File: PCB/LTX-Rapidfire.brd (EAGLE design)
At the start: 62.2 x 46.7 mm, 52 parts, among them J1 F-1X08-SIP-100-40Y, Q1 2N3904, Q10 SS8550D, Q11 2N3906, Q12 2N3906, Q13 2N3904, Q2 2N3906, Q3 2N3904, Q4 2N3904, Q5 2N3904, Q6 2N3906, Q7 2N3906, Q8 2N3906, Q9 2N3904, SW1 F-1X02-SIP-100-40, U2 Z8F082ADIL-8

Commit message: Labeled part numbers in schematic. Prep for SMD-ification
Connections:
- net PA0 renamed RELOAD_BUTTON_PA0
- net PA1 renamed INHIBIT_FILTER_PA1
- net PA2 renamed RESET_PA2
- net PA3 renamed LASERMOD_FILTER_PA3
- net PA4 renamed TODI_FILTER_PA4
- net PA5 renamed TIDO_FILTER_PA5

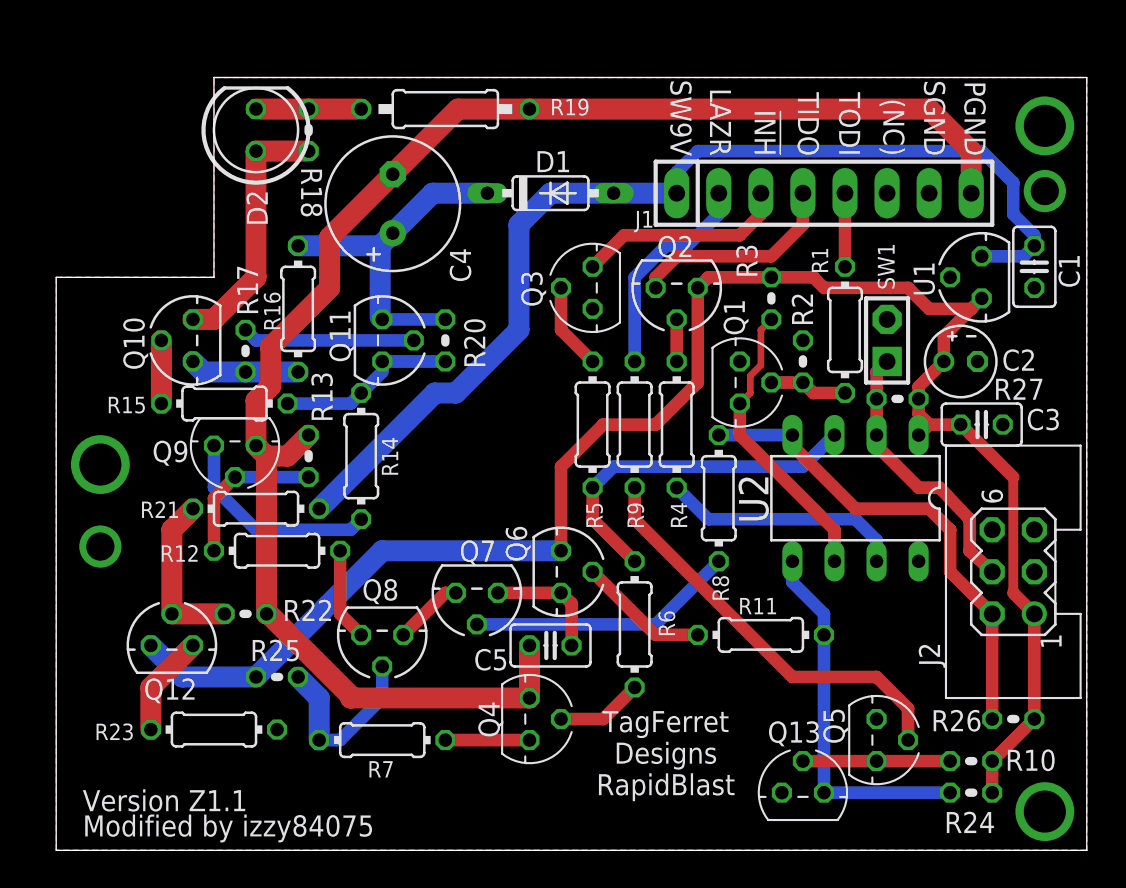
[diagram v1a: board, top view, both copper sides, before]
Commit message: Swapped basics to SMD
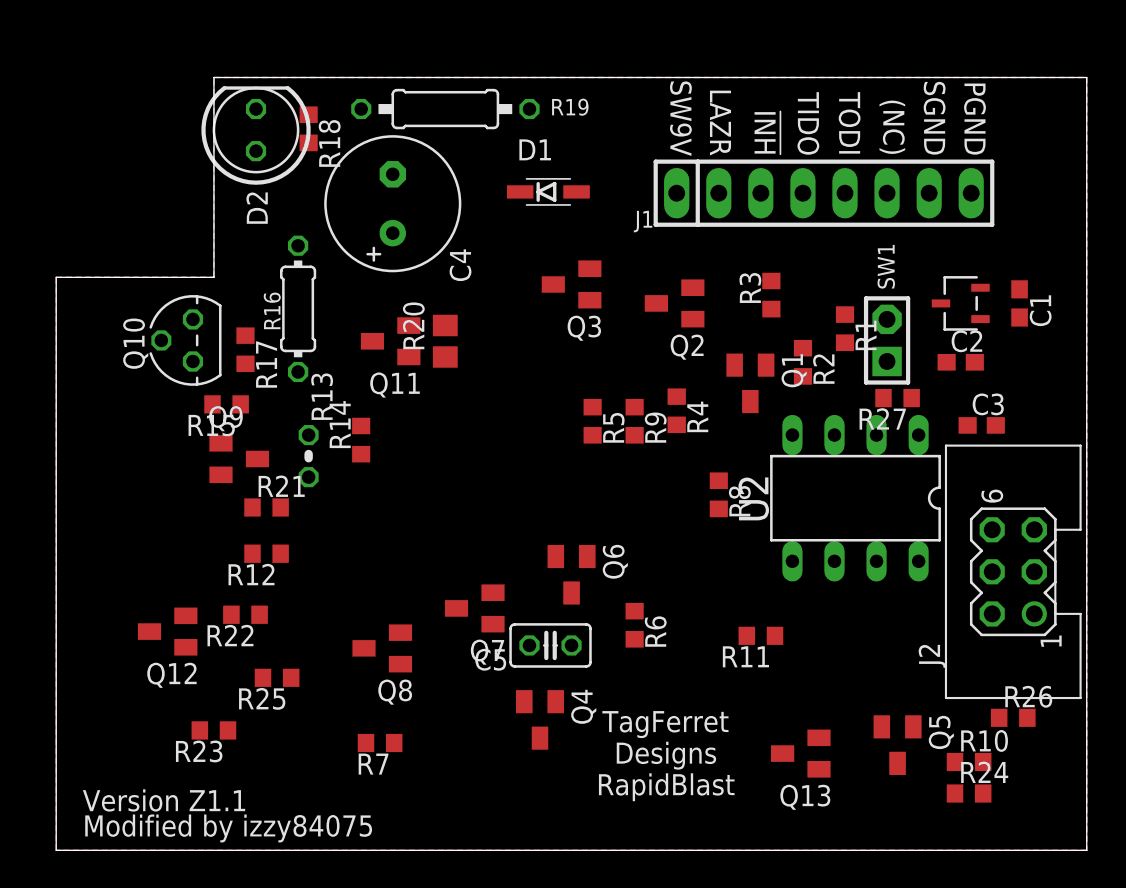
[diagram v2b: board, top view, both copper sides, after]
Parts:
- C1, C3: value 0.1uF -> 100nF; device rcl:C025-025X050 -> JLC PCB Basic Parts_loc:C0603
- C2: value 10uF/10V -> 10uF; device rcl:E2-4 -> JLC PCB Basic Parts_loc:C0603
- D1: value 1N4148DO35-7 -> 1N4148W; device diode:DO35-7 -> JLC PCB Basic Parts_loc:SOD123
- Q1, Q13, Q3, Q4, Q5, Q9: value 2N3904 -> MMBT3904; device transistor:TO92 -> JLC PCB Basic Parts_loc:SOT23
- Q11, Q12, Q2, Q6, Q7, Q8: device transistor-pnp:TO92 -> JLC PCB Basic Parts_loc:SOT23
- R1, R12, R21, R23, R4, R5, R6, R7, R8, R9: device rcl:0204/7 -> JLC PCB Basic Parts_loc:R0603
- R10, R18, R2, R22, R24, R25, R26, R27, R3: device rcl:0204V -> JLC PCB Basic Parts_loc:R0603
- R11: value 1.0k -> 1k; device rcl:0204/7 -> JLC PCB Basic Parts_loc:R0603
- R14: value 150 -> 150R; device rcl:0204/7 -> JLC PCB Basic Parts_loc:R0603
- R15: value 47 -> 47R; device rcl:0204/7 -> JLC PCB Basic Parts_loc:R0603
- R17: value 100 -> 100R; device rcl:0204V -> JLC PCB Basic Parts_loc:R0603
- R20: device rcl:0204V -> JLC PCB Basic Parts_loc:R0805
- U1: value (none) -> XC6206P332MR; device v-reg:78LXX -> LTX-Rapidfire:SOT-23_TOR
- moved C1 2.38 mm to (58.2, 33.0), turned to 270 degrees
- moved Q13 2.37 mm to (45.0, 5.84), turned to 180 degrees
- moved U1 2.02 mm to (54.6, 33.0)
- moved Q5 1.31 mm to (50.8, 6.35)
- moved Q3 1.29 mm to (31.1, 34.2), turned to 180 degrees
- moved R14 0.97 mm to (18.4, 24.8)
- moved Q7 0.95 mm to (25.3, 14.6)
- moved Q2 0.95 mm to (37.3, 33.0)
- moved Q12 0.88 mm to (6.73, 13.2), turned to 180 degrees
- moved Q9 0.85 mm to (11.0, 23.6), turned to 0 degrees
- moved R4 0.84 mm to (37.5, 26.5), turned to 270 degrees
- moved Q8 0.81 mm to (19.7, 12.2)
- moved R12 0.66 mm to (12.7, 17.9), turned to 180 degrees
- moved Q6 0.66 mm to (31.1, 16.6)
- moved R21 0.64 mm to (12.7, 20.7), turned to 0 degrees
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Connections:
- removed net RESET_PA2: J2.2, R26.2, R8.2, U2.4
- removed net TIDO_FILTER_PA5: R4.1, U2.7
- removed net TODI_FILTER_PA4: Q1.1, R3.1, U2.6
- new net PROGRAM_RESET_PA2: J2.2, R26.1, R8.1, U2.4
- new net TIDO_FILTER_TX_PA5: R4.2, U2.7
- new net TODI_FILTER_RX_PA4: Q1.3, R3.1, U2.6
- net INHIBIT: now also Q3.3; no longer Q3.1
- net LASERMOD_FILTER_PA3: now also Q13.3, R11.1; no longer Q13.1, R11.2
- net LAZERMOD: now also R9.1; no longer R9.2
- net N$1: now also Q11.1, R17.1; no longer Q11.2, R17.2
- net N$10: now also Q8.3, R12.1; no longer Q8.1, R12.2
- net N$11: now also Q7.3, Q8.2; no longer Q7.1, Q8.3
- net N$12: now also Q8.1, R7.2; no longer Q8.2, R7.1
- net N$13: now also Q7.1, R8.2; no longer Q7.2, R8.1
- net N$14: now also Q4.3, R7.1; no longer Q4.1, R7.2
- net N$15: now also Q6.3, Q7.2; no longer Q6.1, Q7.3
- net N$16: now also Q4.1; no longer Q4.2
- net N$17: now also Q12.3, R23.2; no longer Q12.1, R23.1
- net N$18: now also Q3.1; no longer Q3.2
- net N$19: now also Q6.1, R11.2; no longer Q6.2, R11.1
- net N$2: now also Q11.2; no longer Q11.3
- net N$20: now also Q12.1, R21.1; no longer Q12.2, R21.2
- net N$21: now also Q13.1, Q5.3; no longer Q13.2, Q5.1
- net N$22: now also Q5.1, R9.2; no longer Q5.2, R9.1
- net N$24: now also Q1.1, R1.2; no longer Q1.2, R1.1
- net N$25: now also Q2.1, R4.1; no longer Q2.2, R4.2
- net N$3: now also R17.2; no longer R17.1
- net N$4: now also Q11.3, R15.1; no longer Q11.1, R15.2
- net N$5: now also R15.2; no longer R15.1
- net N$6: now also Q9.3; no longer Q9.1
- net N$7: now also R18.1; no longer R18.2
- net N$8: now also R18.2; no longer R18.1
- net N$9: now also Q9.1, R12.2; no longer Q9.2, R12.1
- net PGND: now also Q4.2, Q9.2; no longer Q4.3, Q9.3
- net RELOAD_BUTTON_PA0: now also R27.2; no longer R27.1
- net SGND: now also C1.2, C2.2, C3.2, Q1.2, Q13.2, Q3.2, Q5.2, R23.1, U1.1; no longer C1.1, C2.-, C3.1, Q1.3, Q13.3, Q3.3, Q5.3, R23.2, U1.GND
- net SW9V: now also C1.1, R21.2, U1.3; no longer C1.2, R21.1, U1.IN
- net TIDO: now also Q2.3; no longer Q2.1
- net TODI: now also R1.1; no longer R1.2
- net VCC: now also C2.1, C3.1, Q12.2, Q2.2, Q6.2, R26.2, R27.1, U1.2; no longer C2.+, C3.2, Q12.3, Q2.3, Q6.3, R26.1, R27.2, U1.OUT
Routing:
- net VCC: track 104.8 -> 0.00 mm
- net PGND: track 94.7 -> 0.00 mm
- net SW9V: track 63.9 -> 0.00 mm
- net RESET_PA2: track 29.2 -> 0.00 mm
- net N$22: track 25.1 -> 0.00 mm
- net LASERMOD_FILTER_PA3: track 22.4 -> 0.00 mm
- net INHIBIT_FILTER_PA1: track 21.4 -> 0.00 mm
- net N$2: track 21.1 -> 0.00 mm
- net TODI_FILTER_PA4: track 17.8 -> 0.00 mm
- net RELOAD_BUTTON_PA0: track 16.6 -> 0.00 mm
- net N$13: track 16.2 -> 0.00 mm
- net N$8: track 15.7 -> 0.00 mm
- net TIDO_FILTER_PA5: track 14.7 -> 0.00 mm
- net LAZERMOD: track 13.0 -> 0.00 mm
- net INHIBIT: track 12.7 -> 0.00 mm
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- added copper zone on layer 1, net PGND
- removed copper zone on layer 1, net SGND

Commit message: Part lists and gerbers for JLC
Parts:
- C5: value 0.022uF -> 22nF; device rcl:C025-025X050 -> JLC PCB Basic Parts_loc:C0603
- R13: device rcl:0204V -> JLC PCB Basic Parts_loc:R0603
- R16: value 0.62 -> 0.62R 1W; device rcl:0204/7 -> resistor:R2512
- R19: value 3.9 -> 3.9R 1W; device rcl:0207/10 -> resistor:R2512
- moved C4 1.44 mm to (21.3, 38.0)
- moved R19 0.57 mm to (23.6, 44.2)
- moved R16 0.20 mm to (14.6, 32.9)
- moved C5 0.08 mm to (29.8, 12.4)
- moved R13 0.05 mm to (15.2, 23.7), turned to 270 degrees
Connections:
- net N$9: now also R13.2; no longer R13.1
- net PGND: now also R13.1; no longer R13.2
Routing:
- net VCC: track 0.00 -> 133.3 mm
- net SW9V: track 0.00 -> 68.0 mm, vias 0 -> 1
- net SGND: track 0.00 -> 37.2 mm, vias 0 -> 4
- net PROGRAM_RESET_PA2: track 0.00 -> 33.3 mm, vias 0 -> 1
- net PGND: track 0.00 -> 30.6 mm, vias 0 -> 4
- net INHIBIT_FILTER_PA1: track 0.00 -> 27.3 mm, vias 0 -> 2
- net N$22: track 0.00 -> 25.5 mm, vias 0 -> 2
- net LASERMOD_FILTER_PA3: track 0.00 -> 24.8 mm, vias 0 -> 1
- net TIDO_FILTER_TX_PA5: track 0.00 -> 24.1 mm, vias 0 -> 1
- net N$2: track 0.00 -> 23.3 mm
- net TODI_FILTER_RX_PA4: track 0.00 -> 22.0 mm, vias 0 -> 1
- net N$4: track 0.00 -> 20.0 mm
- net N$13: track 0.00 -> 19.1 mm
- net INHIBIT: track 0.00 -> 18.4 mm
- net N$8: track 0.00 -> 16.1 mm
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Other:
- board text added: "9V"
- board text added: "INH"
- board text added: "IR"
- board text added: "MOD"
- board text added: "PGnd"
- board text added: "SGnd"

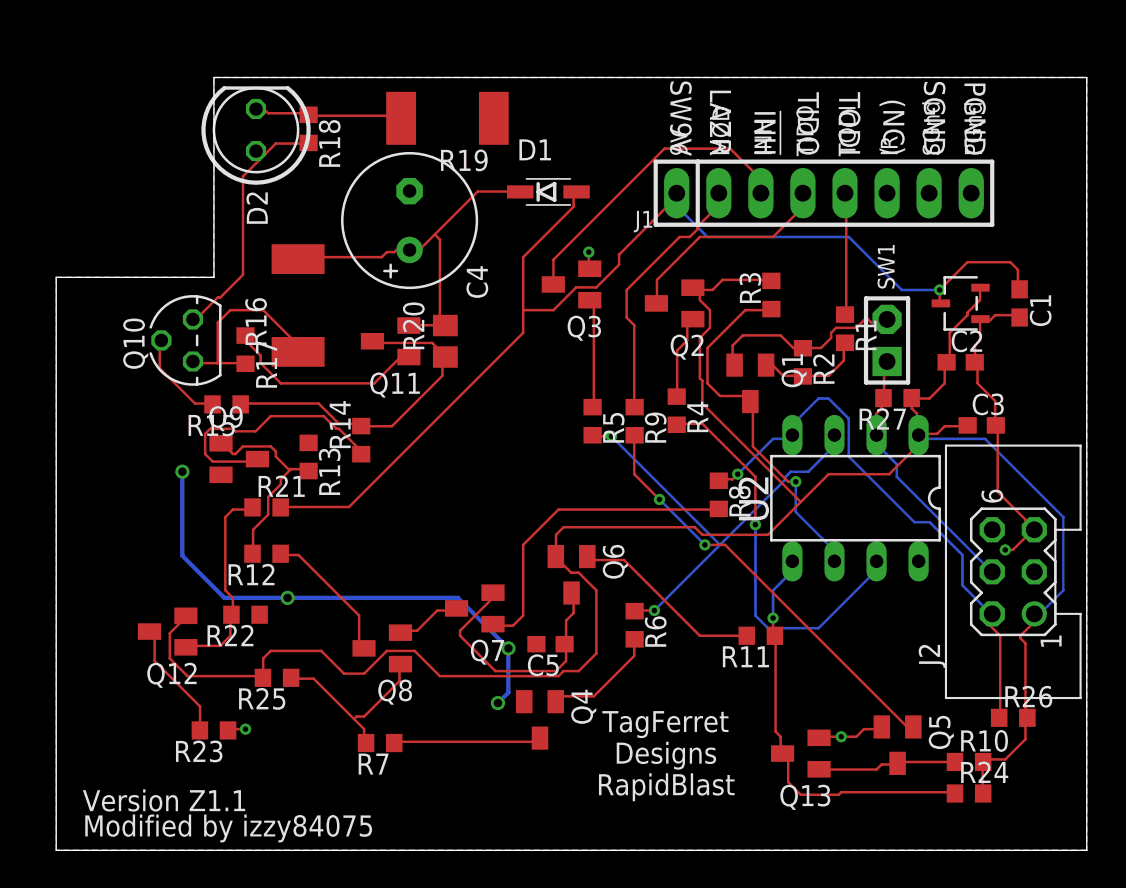
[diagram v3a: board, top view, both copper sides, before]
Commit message: Swapped chip and routed pcb
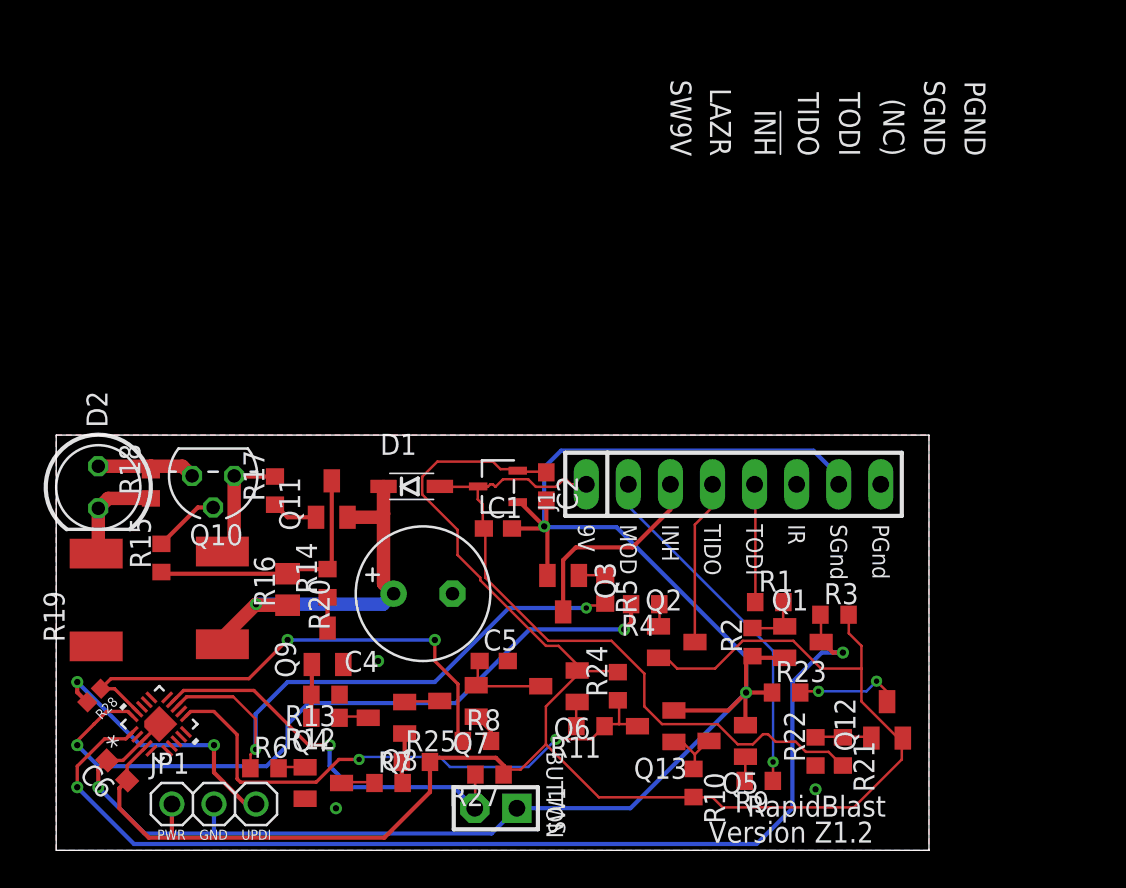
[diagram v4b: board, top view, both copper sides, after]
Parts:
- removed C3: 100nF, JLC PCB Basic Parts_loc:C0603
- removed J2: (no value), izzy:MA03-2
- removed R26: 10k, JLC PCB Basic Parts_loc:R0603
- removed U2: Z8F082ADIL-8, izzy:DIL8
- added C6: 100nF, JLC PCB Basic Parts_loc:C0603
- added JP1: (no value), adafruit:1X03
- added R28: 1K, SparkFun-Resistors:0402
- added U3: ATTINY1616-MNRVQFN20_3X3_MCH-M, attiny1616:VQFN20_3X3_MCH-M
- moved Q12 43.8 mm to (50.2, 7.87), turned to 90 degrees
- moved R21 37.8 mm to (47.5, 5.97), turned to 270 degrees
- moved SW1 36.8 mm to (26.5, 2.54), turned to 180 degrees
- moved R19 36.0 mm to (2.41, 15.1), turned to 90 degrees
- moved R22 35.4 mm to (45.8, 5.97), turned to 90 degrees
- moved R23 34.6 mm to (44.1, 9.53), turned to 0 degrees
- moved C1 34.3 mm to (26.7, 19.4), turned to 0 degrees
- moved R27 33.5 mm to (26.2, 4.57)
- moved U1 30.0 mm to (26.7, 22.0)
- moved C2 26.1 mm to (29.6, 22.0), turned to 270 degrees
- moved R6 24.0 mm to (12.6, 4.95), turned to 0 degrees
- moved D2 23.6 mm to (2.54, 21.9), turned to 270 degrees
- moved R18 23.5 mm to (5.71, 22.1), turned to 90 degrees
- moved R9 23.0 mm to (42.4, 4.19), turned to 180 degrees
- moved C4 22.5 mm to (22.1, 15.5), turned to 0 degrees
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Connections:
- net INHIBIT renamed INHIBIT_OUT
- net LAZERMOD renamed LAZERMOD_IN
- net N$2 renamed PROTECTED_9V
- net SW9V renamed +9V
- removed net INHIBIT_FILTER_PA1: R5.2, R6.1, U2.3
- removed net LASERMOD_FILTER_PA3: Q13.3, R11.1, R24.1, U2.5
- removed net PROGRAM_RESET_PA2: J2.2, R26.1, R8.1, U2.4
- removed net RELOAD_BUTTON_PA0: J2.4, R27.2, SW1.1, U2.2
- removed net TIDO_FILTER_TX_PA5: R4.2, U2.7
- removed net TODI_FILTER_RX_PA4: Q1.3, R3.1, U2.6
- new net INHIBIT_PB1: R5.2, R6.1, U3.13
- new net LASERMOD_IN_PB3: Q13.3, R11.1, R24.1, U3.11
- new net PROGRAM_RESET_PA0: R28.1, R8.1, U3.19
- new net RELOAD_BUTTON_PB0: R27.2, SW1.2, U3.14
- new net TIDO_FILTER_TX_PA1: R4.2, U3.20
- new net TODI_FILTER_RX_PA2: Q1.3, R3.1, U3.1
- new net UPDI: JP1.3, R28.2
- net SGND: now also C6.2, JP1.2, SW1.1, U3.21, U3.3; no longer C3.2, J2.3, J2.5, SW1.2, U2.8
- net VCC: now also C6.1, JP1.1, U3.4; no longer C3.1, J2.1, R26.2, U2.1
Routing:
- net SGND: track 37.2 -> 113.5 mm, vias 4 -> 3
- net TODI_FILTER_RX_PA2: track 0.00 -> 66.1 mm, vias 0 -> 2
- net TIDO_FILTER_TX_PA1: track 0.00 -> 43.9 mm, vias 0 -> 2
- net INHIBIT_PB1: track 0.00 -> 34.7 mm, vias 0 -> 2
- net LASERMOD_IN_PB3: track 0.00 -> 34.2 mm, vias 0 -> 2
- net PROGRAM_RESET_PA2: track 33.3 -> 0.00 mm, vias 1 -> 0
- net PROGRAM_RESET_PA0: track 0.00 -> 31.3 mm, vias 0 -> 2
- net PGND: track 30.6 -> 0.00 mm, vias 4 -> 3
- net INHIBIT_FILTER_PA1: track 27.3 -> 0.00 mm, vias 2 -> 0
- net LASERMOD_FILTER_PA3: track 24.8 -> 0.00 mm, vias 1 -> 0
- net +9V: track 68.0 -> 43.3 mm, vias 1 -> 0
- net RELOAD_BUTTON_PB0: track 0.00 -> 24.7 mm, vias 0 -> 1
- net TIDO_FILTER_TX_PA5: track 24.1 -> 0.00 mm, vias 1 -> 0
- net N$22: track 25.5 -> 1.47 mm, vias 2 -> 0
- net TODI_FILTER_RX_PA4: track 22.0 -> 0.00 mm, vias 1 -> 0
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- added copper zone on layer 16, net PGND
- removed copper zone on layer 16, net SGND
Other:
- board size 62.2 x 46.7 mm -> 52.7 x 25.1 mm
- board text added: "BUTTON"
- board text added: "GND"
- board text added: "PWR"
- board text added: "RapidBlast"
- board text added: "TagFerret"
- board text added: "UPDI"
- board text added: "Version Z1.2"
- board text added: "WestabyElectronics"
- board text added: "izzy84075"
- board text removed: "Modified by izzy84075"
- board text removed: "TagFerret Designs RapidBlast"
- board text removed: "Version Z1.1"
